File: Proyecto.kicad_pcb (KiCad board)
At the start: 2 copper layers, 111.1 x 84.8 mm, 52 parts, among them P1 CONN_01X03, P2 CONN_01X03, Q1 BC808-40, Q2 BC808-40, U1 MCP2515, U2 MCP2551-I/SN, U3 AMS1117, U4 ACS712, U5 ACS712

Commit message: fix tamaños y nuevas librerias
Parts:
- C10, C11, C3, C4, C6, C7, C8, C9, CFilter1, CFliter1: footprint Capacitors_ThroughHole:C_Disc_D3_P2.5 -> w_capacitors:cnp_6mm_disc
- CAN1, S0: footprint Terminal_Blocks:TerminalBlock_Pheonix_MPT-2.54mm_2pol -> w_conn_mkds:mkds_1,5-2
- Crystal2: footprint Crystals:Crystal_HC49-U_Vertical -> w_crystal:crystal_hc-49s
- D_RX1, D_TX1, LED1, LED_Gp1, LED_Gp2, LED_Vcc1: footprint LEDs:LED-5MM -> LEDs:LED-3MM
- ESP8266: footprint Pin_Headers:Pin_Header_Straight_2x04 -> w_pin_strip:pin_socket_4x2
- P1, P2: footprint Terminal_Blocks:TerminalBlock_Pheonix_MPT-2.54mm_3pol -> w_conn_mkds:mkds_1,5-3
- PIN_L1, PIN_R1: footprint Pin_Headers:Pin_Header_Straight_1x15 -> w_pin_strip:pin_socket_2mm_15
- R1, R10, R11, R12, R13, R2, R3, R4, R5, R6, R7, R8, R9: footprint Resistors_ThroughHole:Resistor_Horizontal_RM10mm -> w_pth_resistors:RC05
- moved C9 151.0 mm to (220.9, 75.9), turned to 0 degrees
- moved C10 149.1 mm to (212.9, 84.0), turned to 0 degrees
- moved C7 149.0 mm to (219.4, 69.7), turned to 0 degrees
- moved D_RX1 138.2 mm to (216.1, 60.6)
- moved C8 135.2 mm to (203.7, 93.5), turned to 0 degrees
- moved LED_Vcc1 129.9 mm to (209.0, 60.6)
- moved D_TX1 128.6 mm to (205.0, 78.2)
- moved C4 128.2 mm to (109.2, 180.3), turned to 180 degrees
- moved LED1 121.8 mm to (211.9, 68.7), turned to 0 degrees
- moved C6 121.5 mm to (192.8, 99.6), turned to 0 degrees
- moved Q2 120.4 mm to (95.0, 173.7), turned to 180 degrees
- moved R8 114.4 mm to (185.7, 76.6), turned to 0 degrees
- moved R4 110.1 mm to (91.9, 183.4), turned to 180 degrees
- moved R12 107.4 mm to (200.9, 54.9)
- moved R5 105.7 mm to (170.8, 76.3)
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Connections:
- net pin23 renamed /PIN23
- net pin24 renamed /PIN24
- Carga1 pad 2: Net-(CAN1-Pad1) -> Net-(CAN1-Pad2)
- R5 pad 1: Net-(CAN1-Pad2) -> Net-(CAN1-Pad1)
- S0 pad 1: Net-(S0-Pad1) -> Net-(C6-Pad1)
- U2 pad 6: Net-(CAN1-Pad1) -> Net-(CAN1-Pad2)
- U2 pad 7: Net-(CAN1-Pad2) -> Net-(CAN1-Pad1)
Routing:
- net GND: track 446.8 -> 0.00 mm, vias 6 -> 0
- net +5V: track 429.9 -> 0.00 mm, vias 4 -> 0
- net /AC1: track 64.0 -> 0.00 mm
- net /SCK: track 59.9 -> 0.00 mm
- net /AC2: track 54.5 -> 0.00 mm
- net /3.3V: track 53.1 -> 0.00 mm
- net Net-(D3-Pad2): track 49.2 -> 0.00 mm
- net Net-(R9-Pad2): track 43.0 -> 0.00 mm
- net /PIN23: track 33.2 -> 0.00 mm
- net Net-(R8-Pad2): track 32.9 -> 0.00 mm
- net Net-(C6-Pad1): track 27.4 -> 0.00 mm
- net /CS: track 27.4 -> 0.00 mm
- net Net-(LED_Gp1-Pad1): track 27.0 -> 0.00 mm
- net /PIN24: track 26.9 -> 0.00 mm
- net Net-(CAN1-Pad1): track 25.7 -> 0.00 mm
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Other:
- board outline removed
- net class Default: clearance 0.55 -> 0.2; trace_width 0.3048 -> 0.25; via_dia 1.2 -> 0.6; via_drill 0.8 -> 0.4
- rule trace_clearance: 0.55 -> 0.2
- rule trace_min: 0.3048 -> 0.2
- rule via_min_drill: 0.8 -> 0.3
- rule via_min_size: 1.2 -> 0.4

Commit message: fix
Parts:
- moved CFliter1 147.4 mm to (105.7, 177.8)
- moved R4 14.5 mm to (95.0, 169.2), turned to 90 degrees
- moved Q2 3.70 mm to (91.4, 174.8)
- moved C4 2.09 mm to (109.7, 182.4)
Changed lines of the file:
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@@
   )
   (module w_capacitors:cnp_6mm_disc (layer B.Cu)
-    (at 109.22 180.34 180)
+    (at 109.728 182.372 180)
     (descr "6mm disc ceramic capacitor")
     (tags C)
@@
   )
   (module w_capacitors:cnp_6mm_disc (layer B.Cu)
-    (at 213.93757 77.723)
+    (at 105.664 177.8)
     (descr "6mm disc ceramic capacitor")
     (tags C)
@@
   )
   (module TO_SOT_Packages_SMD:SOT-23 (layer F.Cu)
-    (at 94.996 173.736 180)
+    (at 91.44 174.752 180)
     (descr "SOT-23, Standard")
     (tags SOT-23)
@@
   )
   (module w_pth_resistors:RC05 (layer B.Cu)
-    (at 91.948 183.388 180)
+    (at 94.996 169.164 90)
     (descr "Resistor, RC05")
     (tags R)
     (autoplace_cost180 10)
-    (fp_text reference R4 (at 0 0 180) (layer B.SilkS)
+    (fp_text reference R4 (at 0 0 90) (layer B.SilkS)
       (effects (font (size 1.397 1.27) (thickness 0.2032)) (justify mirror))
     )
-    (fp_text value 1k (at 0 -2.032 180) (layer B.SilkS) hide
+    (fp_text value 1k (at 0 -2.032 90) (layer B.SilkS) hide
       (effects (font (size 1.397 1.27) (thickness 0.2032)) (justify mirror))
     )
@@
     (fp_line (start -5.08 0) (end -4.572 0) (layer B.SilkS) (width 0.3048))
     (fp_line (start 5.08 0) (end 4.572 0) (layer B.SilkS) (width 0.3048))
-    (pad 1 thru_hole circle (at -5.08 0 180) (size 1.99898 1.99898) (drill 0.8001) (layers *.Cu *.Mask B.SilkS)
+    (pad 1 thru_hole circle (at -5.08 0 90) (size 1.99898 1.99898) (drill 0.8001) (layers *.Cu *.Mask B.SilkS)
       (net 56 "Net-(Q2-Pad1)"))
-    (pad 2 thru_hole circle (at 5.08 0 180) (size 1.99898 1.99898) (drill 0.8001) (layers *.Cu *.Mask B.SilkS)
+    (pad 2 thru_hole circle (at 5.08 0 90) (size 1.99898 1.99898) (drill 0.8001) (layers *.Cu *.Mask B.SilkS)
       (net 52 /R1))
     (model walter/pth_resistors/rc05.wrl

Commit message: fix pcb casa
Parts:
- moved C9 158.3 mm to (62.8, 70.5), turned to 180 degrees
- moved D_RX1 147.7 mm to (68.8, 51.2), turned to 90 degrees
- moved C8 141.8 mm to (62.9, 76.4), turned to 180 degrees
- moved C7 138.2 mm to (81.2, 65.9), turned to 180 degrees
- moved D_TX1 130.0 mm to (77.8, 51.1), turned to 90 degrees
- moved C10 129.4 mm to (83.8, 93.0), turned to 270 degrees
- moved LED_Gp2 127.3 mm to (83.3, 107.2)
- moved R12 117.4 mm to (94.0, 103.4), turned to 270 degrees
- moved LED1 112.5 mm to (100.6, 85.1)
- moved R6 112.2 mm to (103.1, 105.0), turned to 180 degrees
- moved R8 111.4 mm to (75.5, 59.8), turned to 270 degrees
- moved LED_Gp1 104.8 mm to (83.6, 100.3)
- moved R5 103.6 mm to (68.0, 90.0), turned to 90 degrees
- moved C6 88.7 mm to (117.3, 53.2), turned to 270 degrees
- moved R7 88.1 mm to (103.1, 101.0), turned to 180 degrees
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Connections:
- LED_Gp1 pad 1: Net-(LED_Gp1-Pad1) -> GND
- LED_Gp1 pad 2: /Gp1 -> Net-(LED_Gp1-Pad2)
- LED_Gp2 pad 1: Net-(LED_Gp2-Pad1) -> GND
- LED_Gp2 pad 2: /Gp2 -> Net-(LED_Gp2-Pad2)
- R6 pad 1: Net-(LED_Gp2-Pad1) -> /Gp2
- R6 pad 2: GND -> Net-(LED_Gp2-Pad2)
- R7 pad 1: Net-(LED_Gp1-Pad1) -> /Gp1
- R7 pad 2: GND -> Net-(LED_Gp1-Pad2)

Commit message: fisx
con 4 puentes... 6.6 cm x12 cm
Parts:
- moved C11 22.1 mm to (157.4, 83.3), turned to 180 degrees
- moved R3 18.9 mm to (136.7, 81.2)
- moved D2 18.8 mm to (145.4, 62.4), turned to 270 degrees
- moved Q1 17.5 mm to (147.2, 81.4), turned to 90 degrees
- moved D_TX1 17.2 mm to (62.5, 58.9), turned to 180 degrees
- moved CFilter1 16.0 mm to (157.1, 80.0), turned to 180 degrees
- moved D_RX1 14.7 mm to (62.5, 64.5), turned to 180 degrees
- moved D1 12.7 mm to (103.3, 54.6)
- moved C7 12.0 mm to (84.1, 54.3)
- moved R4 11.2 mm to (134.6, 95.1), turned to 180 degrees
- moved P1 9.78 mm to (173.8, 67.5)
- moved Relay1 9.78 mm to (150.0, 67.5)
- moved D3 7.67 mm to (147.1, 92.3), turned to 180 degrees
- moved Q2 7.09 mm to (136.5, 100.8)
- moved R8 5.01 mm to (70.6, 58.9), turned to 0 degrees
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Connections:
- Relay1 pad 2: Net-(D2-Pad2) -> +5V
- Relay1 pad 5: +5V -> Net-(D2-Pad2)
- U4 pad 1: Net-(Relay1-Pad1) -> Net-(P1-Pad2)
- U4 pad 2: Net-(Relay1-Pad1) -> Net-(P1-Pad2)
- U4 pad 3: Net-(P1-Pad2) -> Net-(Relay1-Pad1)
- U4 pad 4: Net-(P1-Pad2) -> Net-(Relay1-Pad1)
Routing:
- net GND: track 0.00 -> 451.7 mm, vias 0 -> 4
- net +5V: track 0.00 -> 326.4 mm, vias 0 -> 4
- net Net-(R9-Pad2): track 0.00 -> 57.0 mm
- net /AC2: track 0.00 -> 53.8 mm
- net /SCK: track 0.00 -> 51.3 mm
- net /AC1: track 0.00 -> 46.4 mm
- net /3.3V: track 0.00 -> 46.2 mm
- net Net-(R8-Pad2): track 0.00 -> 39.1 mm
- net Net-(C6-Pad1): track 0.00 -> 37.8 mm
- net Net-(D3-Pad2): track 0.00 -> 33.9 mm
- net /CS: track 0.00 -> 33.7 mm
- net Net-(ESP8266-Pad2): track 0.00 -> 31.9 mm
- net /SO: track 0.00 -> 21.2 mm
- net /SI: track 0.00 -> 20.9 mm
- net /INT: track 0.00 -> 20.3 mm
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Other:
- board outline added: 121 x 73 mm

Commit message: fix
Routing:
- net GND: track 451.7 -> 431.1 mm
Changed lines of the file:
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@@
   (general
     (links 115)
-    (no_connects 0)
+    (no_connects 3)
     (area 57.949999 41.964999 179.050001 115.050001)
     (thickness 1.6)
     (drawings 6)
-    (tracks 421)
+    (tracks 413)
     (zones 0)
     (modules 52)
@@
     (user_trace_width 0.6096)
     (user_trace_width 0.8128)
+    (user_trace_width 0.9144)
+    (user_trace_width 1.016)
     (trace_clearance 0.2)
     (zone_clearance 0.508)
@@
     (via_min_size 0.4)
     (via_min_drill 0.3)
+    (user_via 0.59944 0.39878)
+    (user_via 1.524 0.7874)
     (uvia_size 0.3)
     (uvia_drill 0.1)
@@
   (gr_line (start 58 115) (end 58 49) (angle 90) (layer Edge.Cuts) (width 0.1))
   (gr_line (start 179 115) (end 58 115) (angle 90) (layer Edge.Cuts) (width 0.1))
-  (segment (start 131.729 91.812) (end 131.653 91.888) (width 0.4064) (layer F.Cu) (net 0))
   (segment (start 157.353 58.031) (end 157.438 57.946) (width 0.4064) (layer F.Cu) (net 0))
-  (segment (start 59.944 58.928) (end 59.944 53.4416) (width 0.4064) (layer F.Cu) (net 1) (status 400000))
-  (segment (start 86.614 52.2224) (end 86.614 54.2544) (width 0.4064) (layer F.Cu) (net 1) (status 800000))
+  (segment (start 59.944 58.928) (end 59.944 53.4416) (width 0.4064) (layer F.Cu) (net 1))
+  (segment (start 86.614 52.2224) (end 86.614 54.2544) (width 0.4064) (layer F.Cu) (net 1))
   (segment (start 84.1756 49.784) (end 86.614 52.2224) (width 0.4064) (layer F.Cu) (net 1))
   (segment (start 63.6016 49.784) (end 84.1756 49.784) (width 0.4064) (layer F.Cu) (net 1))
   (segment (start 59.944 53.4416) (end 63.6016 49.784) (width 0.4064) (layer F.Cu) (net 1))
   (segment (start 84.709 62.992) (end 84.709 61.6966) (width 0.4064) (layer F.Cu) (net 1))
-  (segment (start 88.1126 58.293) (end 92.71 58.293) (width 0.4064) (layer F.Cu) (net 1) (status 800000))
+  (segment (start 88.1126 58.293) (end 92.71 58.293) (width 0.4064) (layer F.Cu) (net 1))
   (segment (start 84.709 61.6966) (end 88.1126 58.293) (width 0.4064) (layer F.Cu) (net 1))
-  (segment (start 93.09048 54.60746) (end 86.96706 54.60746) (width 0.4064) (layer F.Cu) (net 1) (status C00000))
-  (segment (start 86.96706 54.60746) (end 86.614 54.2544) (width 0.4064) (layer F.Cu) (net 1) (status C00000))
+  (segment (start 93.09048 54.60746) (end 86.96706 54.60746) (width 0.4064) (layer F.Cu) (net 1))
+  (segment (start 86.96706 54.60746) (end 86.614 54.2544) (width 0.4064) (layer F.Cu) (net 1))
   (segment (start 84.709 62.992) (end 84.709 63.5) (width 0.4064) (layer F.Cu) (net 1))
   (segment (start 84.074 87.63) (end 85.344 88.9) (width 0.4064) (layer F.Cu) (net 1))
@@
   (segment (start 117.22 87.248) (end 121.412 87.248) (width 0.4064) (layer F.Cu) (net 1))
   (segment (start 117.094 87.122) (end 117.22 87.248) (width 0.4064) (layer F.Cu) (net 1))
-  (via (at 117.094 87.122) (size 0.6) (drill 0.4) (layers F.Cu B.Cu) (net 1))
+  (via (at 117.094 87.122) (size 1.524) (drill 0.7874) (layers F.Cu B.Cu) (net 1))
   (segment (start 117.094 64.262) (end 117.094 87.122) (width 0.4064) (layer B.Cu) (net 1))
   (segment (start 114.554 61.722) (end 117.094 64.262) (width 0.4064) (layer B.Cu) (net 1))
-  (via (at 114.554 61.722) (size 0.6) (drill 0.4) (layers F.Cu B.Cu) (net 1))
+  (via (at 114.554 61.722) (size 1.524) (drill 0.7874) (layers F.Cu B.Cu) (net 1))
   (segment (start 114.681 61.595) (end 114.554 61.722) (width 0.4064) (layer F.Cu) (net 1))
   (segment (start 87.885 68.58) (end 87.885 67.055) (width 0.4064) (layer F.Cu) (net 1))
-  (via (at 84.709 62.992) (size 0.6) (drill 0.4) (layers F.Cu B.Cu) (net 1))
+  (via (at 84.709 62.992) (size 1.524) (drill 0.7874) (layers F.Cu B.Cu) (net 1))
   (segment (start 86.36 62.992) (end 84.709 62.992) (width 0.4064) (layer B.Cu) (net 1))
   (segment (start 89.154 65.786) (end 86.36 62.992) (width 0.4064) (layer B.Cu) (net 1))
-  (via (at 89.154 65.786) (size 0.6) (drill 0.4) (layers F.Cu B.Cu) (net 1))
+  (via (at 89.154 65.786) (size 1.524) (drill 0.7874) (layers F.Cu B.Cu) (net 1))
   (segment (start 87.885 67.055) (end 89.154 65.786) (width 0.4064) (layer F.Cu) (net 1))
   (segment (start 160.528 74.041) (end 160.528 71.247) (width 0.4064) (layer F.Cu) (net 1))
@@
   (segment (start 142.2908 110.3884) (end 142.2908 112.649) (width 0.4064) (layer F.Cu) (net 2))
   (segment (start 142.3416 110.3376) (end 142.2908 110.3884) (width 0.4064) (layer F.Cu) (net 2))
-  (via (at 142.3416 110.3376) (size 0.6) (drill 0.4) (layers F.Cu B.Cu) (net 2))
+  (via (at 142.3416 110.3376) (size 1.524) (drill 0.7874) (layers F.Cu B.Cu) (net 2))
   (segment (start 142.3416 90.8812) (end 142.3416 110.3376) (width 0.4064) (layer B.Cu) (net 2))
   (segment (start 145.542 87.6808) (end 142.3416 90.8812) (width 0.4064) (layer B.Cu) (net 2))
-  (via (at 145.542 87.6808) (size 0.6) (drill 0.4) (layers F.Cu B.Cu) (net 2))
+  (via (at 145.542 87.6808) (size 1.524) (drill 0.7874) (layers F.Cu B.Cu) (net 2))
   (segment (start 145.6436 87.5792) (end 145.542 87.6808) (width 0.4064) (layer F.Cu) (net 2))
-  (segment (start 81.534 54.2544) (end 70.2564 54.2544) (width 0.4064) (layer F.Cu) (net 2) (status 400000))
-  (segment (start 62.588 68.072) (end 60.21 70.45) (width 0.4064) (layer F.Cu) (net 2) (status 800000))
+  (segment (start 81.534 54.2544) (end 70.2564 54.2544) (width 0.4064) (layer F.Cu) (net 2))
+  (segment (start 62.588 68.072) (end 60.21 70.45) (width 0.4064) (layer F.Cu) (net 2))
   (segment (start 65.3288 68.072) (end 62.588 68.072) (width 0.4064) (layer F.Cu) (net 2))
   (segment (start 67.564 65.8368) (end 65.3288 68.072) (width 0.4064) (layer F.Cu) (net 2))
@@
   (segment (start 133.144 66.596) (end 135.303 66.596) (width 0.4064) (layer F.Cu) (net 2))
   (segment (start 142.113 76.327) (end 142.113 78.613) (width 0.4064) (layer F.Cu) (net 2))
-  (via (at 142.113 76.327) (size 0.6) (drill 0.4) (layers F.Cu B.Cu) (net 2))
+  (via (at 142.113 76.327) (size 1.524) (drill 0.7874) (layers F.Cu B.Cu) (net 2))
   (segment (start 142.113 73.406) (end 142.113 76.327) (width 0.4064) (layer B.Cu) (net 2))
   (segment (start 137.541 68.834) (end 142.113 73.406) (width 0.4064) (layer B.Cu) (net 2))
-  (via (at 137.541 68.834) (size 0.6) (drill 0.4) (layers F.Cu B.Cu) (net 2))
+  (via (at 137.541 68.834) (size 1.524) (drill 0.8) (layers F.Cu B.Cu) (net 2))
   (segment (start 135.303 66.596) (end 137.541 68.834) (width 0.4064) (layer F.Cu) (net 2))
   (segment (start 142.113 78.613) (end 142.113 78.486) (width 0.4064) (layer F.Cu) (net 2))
@@
   (segment (start 61.087 100.584) (end 73.914 100.584) (width 0.4064) (layer F.Cu) (net 2))
   (segment (start 60.35 99.847) (end 61.087 100.584) (width 0.4064) (layer F.Cu) (net 2))
-  (segment (start 84.328 100.584) (end 78.232 100.584) (width 0.4064) (layer F.Cu) (net 2))
-  (segment (start 78.232 100.584) (end 76.073 98.425) (width 0.4064) (layer F.Cu) (net 2))
   (segment (start 76.073 98.425) (end 76.073 93.345) (width 0.4064) (layer F.Cu) (net 2))
   (segment (start 86.868 84.836) (end 86.868 86.995) (width 0.4064) (layer F.Cu) (net 2))
@@
   (segment (start 89.28 87.248) (end 86.868 84.836) (width 0.4064) (layer F.Cu) (net 2))
   (segment (start 85.344 93.98) (end 87.757 93.98) (width 0.4064) (layer F.Cu) (net 2))
-  (segment (start 87.757 93.98) (end 87.884 93.98) (width 0.4064) (layer F.Cu) (net 2))
-  (segment (start 87.884 93.98) (end 90.932 97.028) (width 0.4064) (layer F.Cu) (net 2))
-  (segment (start 84.328 100.584) (end 84.328 96.901) (width 0.4064) (layer F.Cu) (net 2))
-  (segment (start 85.344 95.885) (end 85.344 93.98) (width 0.4064) (layer F.Cu) (net 2))
-  (segment (start 84.328 96.901) (end 85.344 95.885) (width 0.4064) (layer F.Cu) (net 2))
   (segment (start 84.328 105.156) (end 84.328 100.584) (width 0.4064) (layer F.Cu) (net 2))
   (segment (start 133.144 70.628) (end 133.144 66.596) (width 0.4064) (layer F.Cu) (net 2))
@@
   (segment (start 76.073 58.928) (end 78.485 61.34) (width 0.4064) (layer F.Cu) (net 56))
   (segment (start 78.485 61.34) (end 78.485 68.58) (width 0.4064) (layer F.Cu) (net 56))
-  (segment (start 75.184 64.516) (end 75.184 64.1096) (width 0.4064) (layer F.Cu) (net 57) (status C00000))
-  (segment (start 75.184 64.1096) (end 71.4756 60.4012) (width 0.4064) (layer F.Cu) (net 57) (status 400000))
+  (segment (start 75.184 64.516) (end 75.184 64.1096) (width 0.4064) (layer F.Cu) (net 57))
+  (segment (start 75.184 64.1096) (end 71.4756 60.4012) (width 0.4064) (layer F.Cu) (net 57))
   (segment (start 82.423 63.4238) (end 82.1436 63.1444) (width 0.4064) (layer F.Cu) (net 57))
   (segment (start 82.1436 63.1444) (end 81.1784 63.1444) (width 0.4064) (layer F.Cu) (net 57))

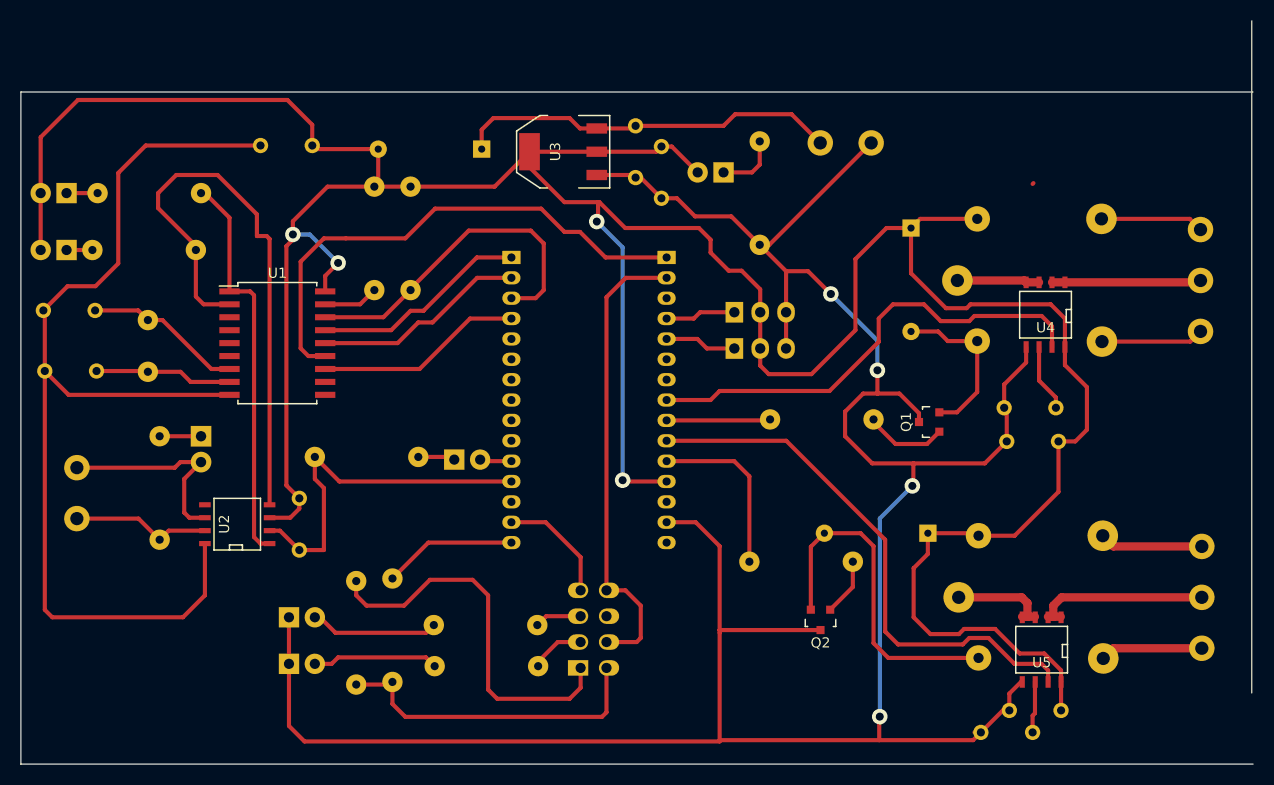
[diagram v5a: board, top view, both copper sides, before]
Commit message: fix
achicamiento 6.5 x 10.7 cm
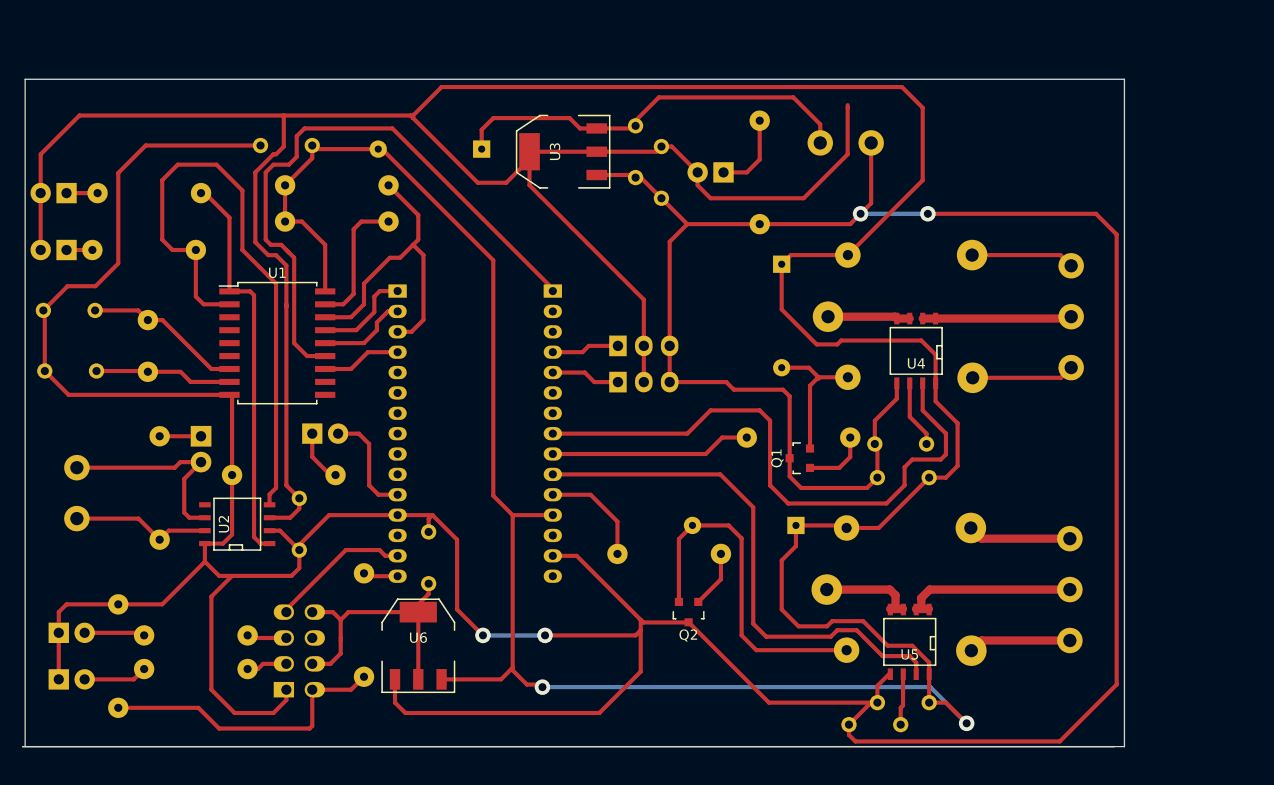
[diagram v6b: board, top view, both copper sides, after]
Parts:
- added C12: 100nf, w_capacitors:cnp_6mm_disc, B.Cu at (98.0, 94.7)
- added U6: AMS1117, TO_SOT_Packages_SMD:SOT-223, F.Cu at (97.0, 103.4)
- moved ESP8266 29.0 mm to (85.3, 103.9)
- moved R6 28.5 mm to (75.2, 105.7)
- moved R7 28.5 mm to (75.2, 102.4)
- moved R13 23.5 mm to (67.6, 104.4)
- moved LED_Gp1 22.7 mm to (61.7, 102.1)
- moved LED_Gp2 22.7 mm to (61.7, 106.7)
- moved LED1 14.2 mm to (86.6, 82.5)
- moved C11 13.2 mm to (144.7, 86.9)
- moved P1 13.2 mm to (161.1, 71.1)
- moved Q1 13.2 mm to (134.5, 85.0)
- moved Relay1 13.2 mm to (137.3, 71.1)
- moved CFilter1 13.2 mm to (144.4, 83.6)
- moved D2 13.2 mm to (132.7, 65.9)
- moved U4 13.2 mm to (145.9, 74.4)
- moved C4 13.0 mm to (144.7, 109.0)
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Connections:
- ESP8266 pad 4: /3.3V -> +3.3V
- ESP8266 pad 8: /3.3V -> +3.3V
- PIN_R1 pad 2: /3.3V -> Net-(PIN_R1-Pad2)
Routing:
- net +5V: track 326.4 -> 481.5 mm, vias 4 -> 2
- net /3.3V: track 46.2 -> 0.00 mm
- net +3.3V: track 0.00 -> 27.7 mm
- net GND: track 431.1 -> 454.3 mm
- net /INT: track 20.3 -> 7.79 mm
- net /SI: track 20.9 -> 8.85 mm
- net /SO: track 21.2 -> 9.59 mm
- net /AC1: track 46.4 -> 58.0 mm
- net Net-(PIN_L1-Pad15): track 13.1 -> 3.42 mm
- net /R2: track 10.2 -> 19.7 mm
- net /SCK: track 51.3 -> 60.4 mm
- net Net-(R1-Pad2): track 5.40 -> 13.3 mm
- net /LED: track 3.13 -> 10.7 mm
- net /R1: track 17.1 -> 10.6 mm
- net Net-(LED_Gp1-Pad2): track 12.6 -> 6.46 mm
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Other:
- board size 121 x 73 mm -> 108.2 x 65.5 mm
